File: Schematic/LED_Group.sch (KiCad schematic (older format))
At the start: 21 parts

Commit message: V1.1.0 Realized that while the TLS5940 PWM Driver chip is using the SPI MOSI and SCK signals, the full signaling isn't SPI compatable. Specifically, the latch signal is high active where SPI CS is low active. Removed the SPI cleverness that allows many SPI devices with only 2 CS pins and daisy-chaned all 26 TLS5940s. Also changed the I/O Expander from SPI to I2C. Still need to decide on how to properly handle the unused PWM Driver outputs to keep the internal constant current channels from trying to pump current through and open circuit. Maybe add back-side LEDs for status signals? Also need to watch out for problems driving that many drivers. Might need to split up the groups between multiple µPs. Never the less, should be ready for prototype stage at this point.
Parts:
- gave numbers to parts that had none: 19
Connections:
- net labels added: BLANK', GSCLK', SCK', SIN, SOUT, XLAT, XLAT', ~IR_LED
- net labels removed: IR_LED, MOSI, ~CS~/XLAT
- wire segments 71 -> 178
- no-connect marks 5 -> 9
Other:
- moved on the sheet: C201, C202, C203, D210, R201, R202, R203, U203

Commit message: 1.1.1 Change TIP120 to TIP31C (on-hand stock), change Cap Ref'ds on LED Groups Fritzing file to plan perfboard layout for LED groups.
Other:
- moved on the sheet: C1101, C1102, C1103

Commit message: Updated schematic for simplified auto-cycling leds. Lower part count and cost, not as flexible on color cycling.
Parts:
- removed C201, C202: 0.1µF, symbol CAP_NP
- removed D201, D202, D203, D204, D205, D206, D207, D208, D209: SparkFun COM-10821, symbol LED_RABG
- removed R201, R202: 1.91kΩ, symbol RES
- removed U201, U202: TLC5940NT, symbol TLC5940NT
- added D301, D302, D303, D304, D305, D306, D307, D308, D309: RGB Slow Flashing, symbol LED_Flashing
- added Q301: 2N2222, symbol Q_NPN_EBC
- added R301, R302, R303, R304, R305, R306, R307, R308, R309: 180Ω, symbol RES
- added R310: 1kΩ, symbol RES
- R311: renamed from R203; value 75Ω -> 180Ω
- renumbered C203 to C301, D210 to D310, U203 to U301
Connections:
- net labels added: Blue, Blue/White, Brown, Brown/White, Green, Green/White, IR_5V, IR_GND, LED, LED_5V, LED_GND1, LED_GND3, Orange, Orange/White
- net labels removed: BLANK, BLANK', GND, GSCLK, GSCLK', SCK, SCK', SIN, SOUT, XLAT, XLAT'
- wire segments 178 -> 52
- no-connect marks 9 -> 0
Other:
- note added: "LED Voltage Drop, 2.28V - 2.91V (Max current = 20mA)\n2N2222 Voltage Drop 17.8mV - 15.1mV\nResustor Voltage Drop 2.57 - 2.00V\n\nTarget current = 15mA for a total of 1.755A with 117 LEDs"
- moved on the sheet: C1101, D1110, R1111, U1101

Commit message: Change TIP31C to 2N2222. (Don't need the current capacity, so why pay for it?) Clean-up BOM items.
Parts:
- D301, D302, D303, D304, D305, D306, D307, D308, D309: CommonPartLibrary CPL-LED-RGP-CYCLING-SLOW* -> CPL-LED-RGB-CYCLING-SLOW*
- D310: CommonPartLibrary CPL-LED-5MM-IR -> CPL-LED-5MM-IR*
- R301, R302, R303, R304, R305, R306, R307, R308, R309: CommonPartLibrary CPL-RES-THT-180-0.25W -> CPL-RES-THT-180-0.25W*; MfgPart MFR-25FBF52-10R -> MFR-25FBF52-180R
- R310: MfgPart MFR-25FBF52-1k -> MFR-25FBF52-1K
- R311: CommonPartLibrary CPL-RES-THT-75.0-0.25W -> CPL-RES-THT-180-0.25W*; MfgPart MFR-25FBF52-75R -> MFR-25FBF52-180R
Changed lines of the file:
@@
 Sheet 11 15
 Title "Interactive Rainbow"
-Date "2015-12-05"
-Rev "1.2.0"
+Date "2015-12-06"
+Rev "1.2.1"
 Comp "Sembazuru Circuit (for Barrel of Makers)"
-Comment1 "1.0.0 Initial Circuit"
-Comment2 "1.1.0 TLC5940 isn't actually SPI. Removed SPI cleverness and change I/O expander to I2C"
-Comment3 "1.1.1 Change TIP120 to TIP31C (on-hand stock), change Cap Ref'ds on LED Groups"
-Comment4 "1.2.0 Change design to use LEDs with integrated flashing. Simpler design."
+Comment1 "1.1.0 TLC5940 isn't actually SPI. Removed SPI cleverness and change I/O expander to I2C"
+Comment2 "1.1.1 Change TIP120 to TIP31C (on-hand stock), change Cap Ref'ds on LED Groups"
+Comment3 "1.2.0 Change design to use LEDs with integrated flashing. Simpler design."
+Comment4 "1.2.1 Chance TIP31C to 2N2222. Don't need extra current capacity."
 $EndDescr
 Text HLabel 1050 4700 0    60   Input ~ 0
@@
 F 2 "" H 2100 4700 60  0001 C CNN
 F 3 "" H 2200 4800 60  0001 C CNN
-F 4 "CPL-LED-5MM-IR" H 2200 4700 60  0001 C CNN "CommonPartLibrary"
+F 4 "CPL-LED-5MM-IR*" H 2200 4700 60  0001 C CNN "CommonPartLibrary"
 F 5 "Vishay" H 2200 4700 60  0001 C CNN "Mfg"
 F 6 "TSUS5202" H 2200 4700 60  0001 C CNN "MfgPart"
@@
 F 2 "" H 3100 5350 60  0000 C CNN
 F 3 "" H 3100 5350 60  0000 C CNN
-F 4 "CPL-RES-THT-75.0-0.25W" H 3100 5350 60  0001 C CNN "CommonPartLibrary"
+F 4 "CPL-RES-THT-180-0.25W*" H 3100 5350 60  0001 C CNN "CommonPartLibrary"
 F 5 "Yageo" H 3100 5350 60  0001 C CNN "Mfg"
-F 6 "MFR-25FBF52-75R" H 3100 5350 60  0001 C CNN "MfgPart"
+F 6 "MFR-25FBF52-180R" H 3100 5350 60  0001 C CNN "MfgPart"
 	1    3100 5350
 	1    0    0    -1
@@
 F 2 "" H 5200 1800 60  0001 C CNN
 F 3 "" H 5300 1700 60  0001 C CNN
-F 4 "CPL-LED-RGP-CYCLING-SLOW*" H 5300 1650 60  0001 C CNN "CommonPartLibrary"
+F 4 "CPL-LED-RGB-CYCLING-SLOW*" H 5300 1650 60  0001 C CNN "CommonPartLibrary"
 F 5 "AdaFruit" H 5300 1650 60  0001 C CNN "Mfg"
 F 6 "ADA679" H 5300 1650 60  0001 C CNN "MfgPart"
@@
 F 4 "CPL-RES-THT-1k-0.25W" H 2800 2650 60  0001 C CNN "CommonPartLibrary"
 F 5 "Yageo" H 2800 2650 60  0001 C CNN "Mfg"
-F 6 "MFR-25FBF52-1k" H 2800 2650 60  0001 C CNN "MfgPart"
+F 6 "MFR-25FBF52-1K" H 2800 2650 60  0001 C CNN "MfgPart"
 	1    2800 2650
 	1    0    0    -1
@@
 F 2 "" H 5300 1050 60  0000 C CNN
 F 3 "" H 5300 1050 60  0000 C CNN
-F 4 "CPL-RES-THT-180-0.25W" H 5300 1050 60  0001 C CNN "CommonPartLibrary"
+F 4 "CPL-RES-THT-180-0.25W*" H 5300 1050 60  0001 C CNN "CommonPartLibrary"
 F 5 "Yageo" H 5300 1050 60  0001 C CNN "Mfg"
-F 6 "MFR-25FBF52-10R" H 5300 1050 60  0001 C CNN "MfgPart"
+F 6 "MFR-25FBF52-180R" H 5300 1050 60  0001 C CNN "MfgPart"
 	1    5300 1050
 	0    1    1    0
@@
 F 2 "" H 7200 1800 60  0001 C CNN
 F 3 "" H 7300 1700 60  0001 C CNN
-F 4 "CPL-LED-RGP-CYCLING-SLOW*" H 7300 1650 60  0001 C CNN "CommonPartLibrary"
+F 4 "CPL-LED-RGB-CYCLING-SLOW*" H 7300 1650 60  0001 C CNN "CommonPartLibrary"
 F 5 "AdaFruit" H 7300 1650 60  0001 C CNN "Mfg"
 F 6 "ADA679" H 7300 1650 60  0001 C CNN "MfgPart"
@@
 F 2 "" H 7300 1050 60  0000 C CNN
 F 3 "" H 7300 1050 60  0000 C CNN
-F 4 "CPL-RES-THT-180-0.25W" H 7300 1050 60  0001 C CNN "CommonPartLibrary"
+F 4 "CPL-RES-THT-180-0.25W*" H 7300 1050 60  0001 C CNN "CommonPartLibrary"
 F 5 "Yageo" H 7300 1050 60  0001 C CNN "Mfg"
-F 6 "MFR-25FBF52-10R" H 7300 1050 60  0001 C CNN "MfgPart"
+F 6 "MFR-25FBF52-180R" H 7300 1050 60  0001 C CNN "MfgPart"
 	1    7300 1050
 	0    1    1    0
@@
 F 2 "" H 9200 1800 60  0001 C CNN
 F 3 "" H 9300 1700 60  0001 C CNN
-F 4 "CPL-LED-RGP-CYCLING-SLOW*" H 9300 1650 60  0001 C CNN "CommonPartLibrary"
+F 4 "CPL-LED-RGB-CYCLING-SLOW*" H 9300 1650 60  0001 C CNN "CommonPartLibrary"
 F 5 "AdaFruit" H 9300 1650 60  0001 C CNN "Mfg"
 F 6 "ADA679" H 9300 1650 60  0001 C CNN "MfgPart"
@@
 F 2 "" H 9300 1050 60  0000 C CNN
 F 3 "" H 9300 1050 60  0000 C CNN
-F 4 "CPL-RES-THT-180-0.25W" H 9300 1050 60  0001 C CNN "CommonPartLibrary"
+F 4 "CPL-RES-THT-180-0.25W*" H 9300 1050 60  0001 C CNN "CommonPartLibrary"
 F 5 "Yageo" H 9300 1050 60  0001 C CNN "Mfg"
-F 6 "MFR-25FBF52-10R" H 9300 1050 60  0001 C CNN "MfgPart"
+F 6 "MFR-25FBF52-180R" H 9300 1050 60  0001 C CNN "MfgPart"
 	1    9300 1050
 	0    1    1    0
@@
 F 2 "" H 5200 3800 60  0001 C CNN
 F 3 "" H 5300 3700 60  0001 C CNN
-F 4 "CPL-LED-RGP-CYCLING-SLOW*" H 5300 3650 60  0001 C CNN "CommonPartLibrary"
+F 4 "CPL-LED-RGB-CYCLING-SLOW*" H 5300 3650 60  0001 C CNN "CommonPartLibrary"
 F 5 "AdaFruit" H 5300 3650 60  0001 C CNN "Mfg"
 F 6 "ADA679" H 5300 3650 60  0001 C CNN "MfgPart"
@@
 F 2 "" H 5300 3050 60  0000 C CNN
 F 3 "" H 5300 3050 60  0000 C CNN
-F 4 "CPL-RES-THT-180-0.25W" H 5300 3050 60  0001 C CNN "CommonPartLibrary"
+F 4 "CPL-RES-THT-180-0.25W*" H 5300 3050 60  0001 C CNN "CommonPartLibrary"
 F 5 "Yageo" H 5300 3050 60  0001 C CNN "Mfg"
-F 6 "MFR-25FBF52-10R" H 5300 3050 60  0001 C CNN "MfgPart"
+F 6 "MFR-25FBF52-180R" H 5300 3050 60  0001 C CNN "MfgPart"
 	1    5300 3050
 	0    1    1    0
@@
 F 2 "" H 7200 3800 60  0001 C CNN
 F 3 "" H 7300 3700 60  0001 C CNN
-F 4 "CPL-LED-RGP-CYCLING-SLOW*" H 7300 3650 60  0001 C CNN "CommonPartLibrary"
+F 4 "CPL-LED-RGB-CYCLING-SLOW*" H 7300 3650 60  0001 C CNN "CommonPartLibrary"
 F 5 "AdaFruit" H 7300 3650 60  0001 C CNN "Mfg"
 F 6 "ADA679" H 7300 3650 60  0001 C CNN "MfgPart"
@@
 F 2 "" H 7300 3050 60  0000 C CNN
 F 3 "" H 7300 3050 60  0000 C CNN
-F 4 "CPL-RES-THT-180-0.25W" H 7300 3050 60  0001 C CNN "CommonPartLibrary"
+F 4 "CPL-RES-THT-180-0.25W*" H 7300 3050 60  0001 C CNN "CommonPartLibrary"
 F 5 "Yageo" H 7300 3050 60  0001 C CNN "Mfg"
-F 6 "MFR-25FBF52-10R" H 7300 3050 60  0001 C CNN "MfgPart"
+F 6 "MFR-25FBF52-180R" H 7300 3050 60  0001 C CNN "MfgPart"
 	1    7300 3050
 	0    1    1    0
@@
 F 2 "" H 9200 3800 60  0001 C CNN
 F 3 "" H 9300 3700 60  0001 C CNN
-F 4 "CPL-LED-RGP-CYCLING-SLOW*" H 9300 3650 60  0001 C CNN "CommonPartLibrary"
+F 4 "CPL-LED-RGB-CYCLING-SLOW*" H 9300 3650 60  0001 C CNN "CommonPartLibrary"
 F 5 "AdaFruit" H 9300 3650 60  0001 C CNN "Mfg"
 F 6 "ADA679" H 9300 3650 60  0001 C CNN "MfgPart"
@@
 F 2 "" H 9300 3050 60  0000 C CNN
 F 3 "" H 9300 3050 60  0000 C CNN
-F 4 "CPL-RES-THT-180-0.25W" H 9300 3050 60  0001 C CNN "CommonPartLibrary"
+F 4 "CPL-RES-THT-180-0.25W*" H 9300 3050 60  0001 C CNN "CommonPartLibrary"
 F 5 "Yageo" H 9300 3050 60  0001 C CNN "Mfg"
-F 6 "MFR-25FBF52-10R" H 9300 3050 60  0001 C CNN "MfgPart"
+F 6 "MFR-25FBF52-180R" H 9300 3050 60  0001 C CNN "MfgPart"
 	1    9300 3050
 	0    1    1    0
@@
 F 2 "" H 5200 5800 60  0001 C CNN
 F 3 "" H 5300 5700 60  0001 C CNN
-F 4 "CPL-LED-RGP-CYCLING-SLOW*" H 5300 5650 60  0001 C CNN "CommonPartLibrary"
+F 4 "CPL-LED-RGB-CYCLING-SLOW*" H 5300 5650 60  0001 C CNN "CommonPartLibrary"
 F 5 "AdaFruit" H 5300 5650 60  0001 C CNN "Mfg"
 F 6 "ADA679" H 5300 5650 60  0001 C CNN "MfgPart"
@@
 F 2 "" H 5300 5050 60  0000 C CNN
 F 3 "" H 5300 5050 60  0000 C CNN
-F 4 "CPL-RES-THT-180-0.25W" H 5300 5050 60  0001 C CNN "CommonPartLibrary"
+F 4 "CPL-RES-THT-180-0.25W*" H 5300 5050 60  0001 C CNN "CommonPartLibrary"
 F 5 "Yageo" H 5300 5050 60  0001 C CNN "Mfg"
-F 6 "MFR-25FBF52-10R" H 5300 5050 60  0001 C CNN "MfgPart"
+F 6 "MFR-25FBF52-180R" H 5300 5050 60  0001 C CNN "MfgPart"
 	1    5300 5050
 	0    1    1    0
@@
 F 2 "" H 7200 5800 60  0001 C CNN
 F 3 "" H 7300 5700 60  0001 C CNN
-F 4 "CPL-LED-RGP-CYCLING-SLOW*" H 7300 5650 60  0001 C CNN "CommonPartLibrary"
+F 4 "CPL-LED-RGB-CYCLING-SLOW*" H 7300 5650 60  0001 C CNN "CommonPartLibrary"
 F 5 "AdaFruit" H 7300 5650 60  0001 C CNN "Mfg"
 F 6 "ADA679" H 7300 5650 60  0001 C CNN "MfgPart"
@@
 F 2 "" H 7300 5050 60  0000 C CNN
 F 3 "" H 7300 5050 60  0000 C CNN
-F 4 "CPL-RES-THT-180-0.25W" H 7300 5050 60  0001 C CNN "CommonPartLibrary"
+F 4 "CPL-RES-THT-180-0.25W*" H 7300 5050 60  0001 C CNN "CommonPartLibrary"
 F 5 "Yageo" H 7300 5050 60  0001 C CNN "Mfg"
-F 6 "MFR-25FBF52-10R" H 7300 5050 60  0001 C CNN "MfgPart"
+F 6 "MFR-25FBF52-180R" H 7300 5050 60  0001 C CNN "MfgPart"
 	1    7300 5050
 	0    1    1    0
@@
 F 2 "" H 9200 5800 60  0001 C CNN
 F 3 "" H 9300 5700 60  0001 C CNN
-F 4 "CPL-LED-RGP-CYCLING-SLOW*" H 9300 5650 60  0001 C CNN "CommonPartLibrary"
+F 4 "CPL-LED-RGB-CYCLING-SLOW*" H 9300 5650 60  0001 C CNN "CommonPartLibrary"
 F 5 "AdaFruit" H 9300 5650 60  0001 C CNN "Mfg"
 F 6 "ADA679" H 9300 5650 60  0001 C CNN "MfgPart"
@@
 F 2 "" H 9300 5050 60  0000 C CNN
 F 3 "" H 9300 5050 60  0000 C CNN
-F 4 "CPL-RES-THT-180-0.25W" H 9300 5050 60  0001 C CNN "CommonPartLibrary"
+F 4 "CPL-RES-THT-180-0.25W*" H 9300 5050 60  0001 C CNN "CommonPartLibrary"
 F 5 "Yageo" H 9300 5050 60  0001 C CNN "Mfg"
-F 6 "MFR-25FBF52-10R" H 9300 5050 60  0001 C CNN "MfgPart"
+F 6 "MFR-25FBF52-180R" H 9300 5050 60  0001 C CNN "MfgPart"
 	1    9300 5050
 	0    1    1    0

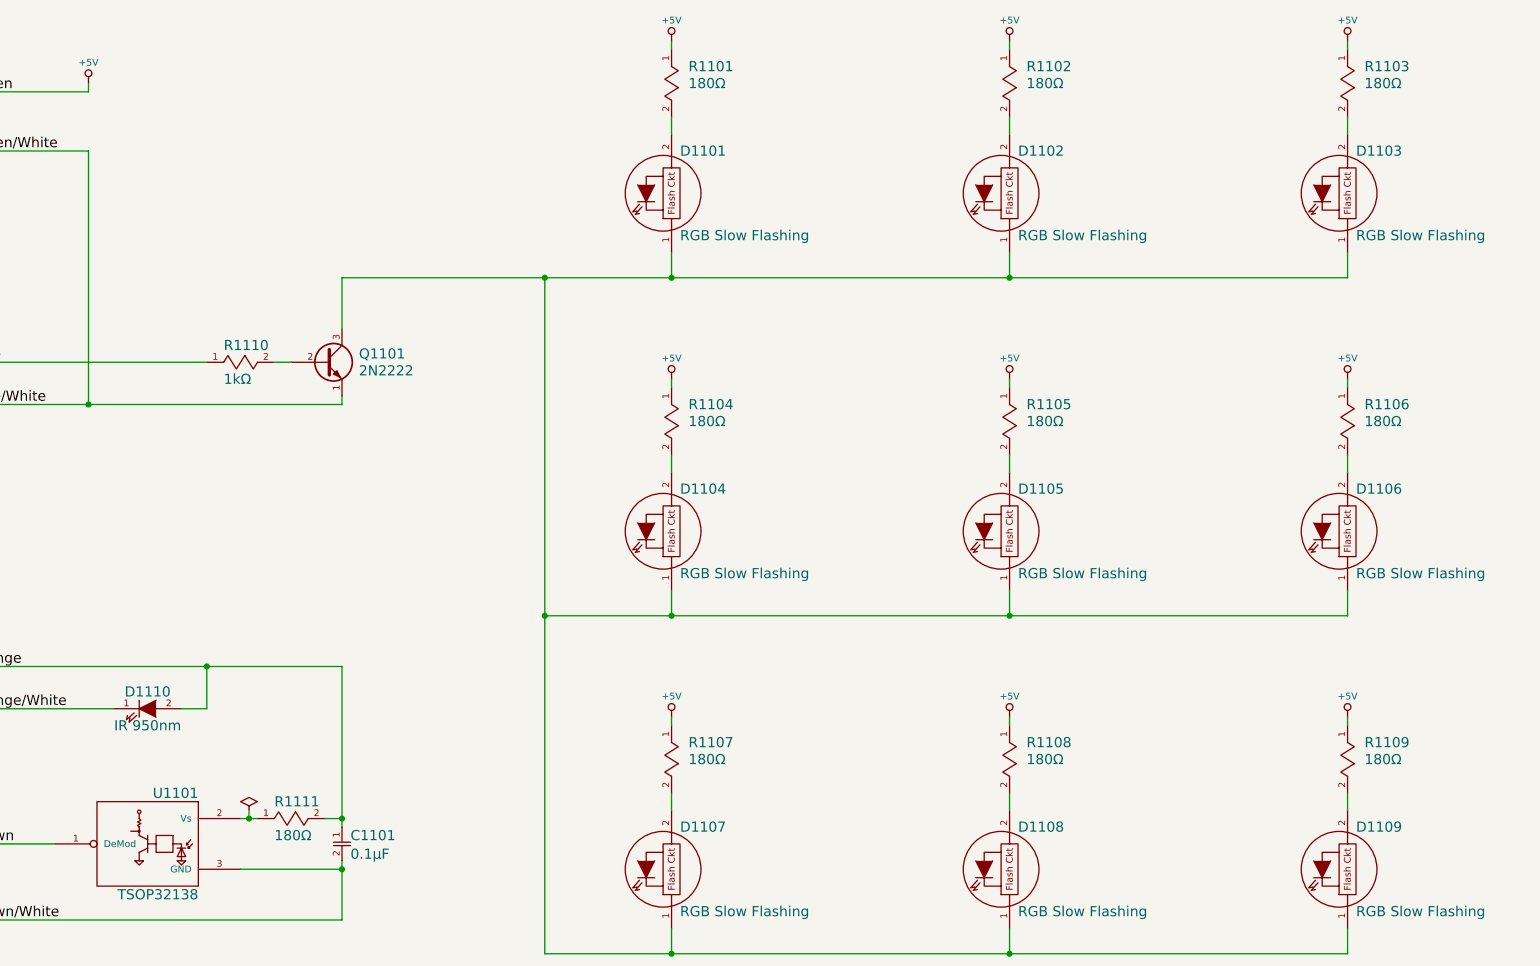
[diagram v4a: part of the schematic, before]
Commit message: v1.2.2 Change 555 to CMOS 7555 to simplify IR strobe design & lower current. And, control IR LEDs to only light when SPI transfer.
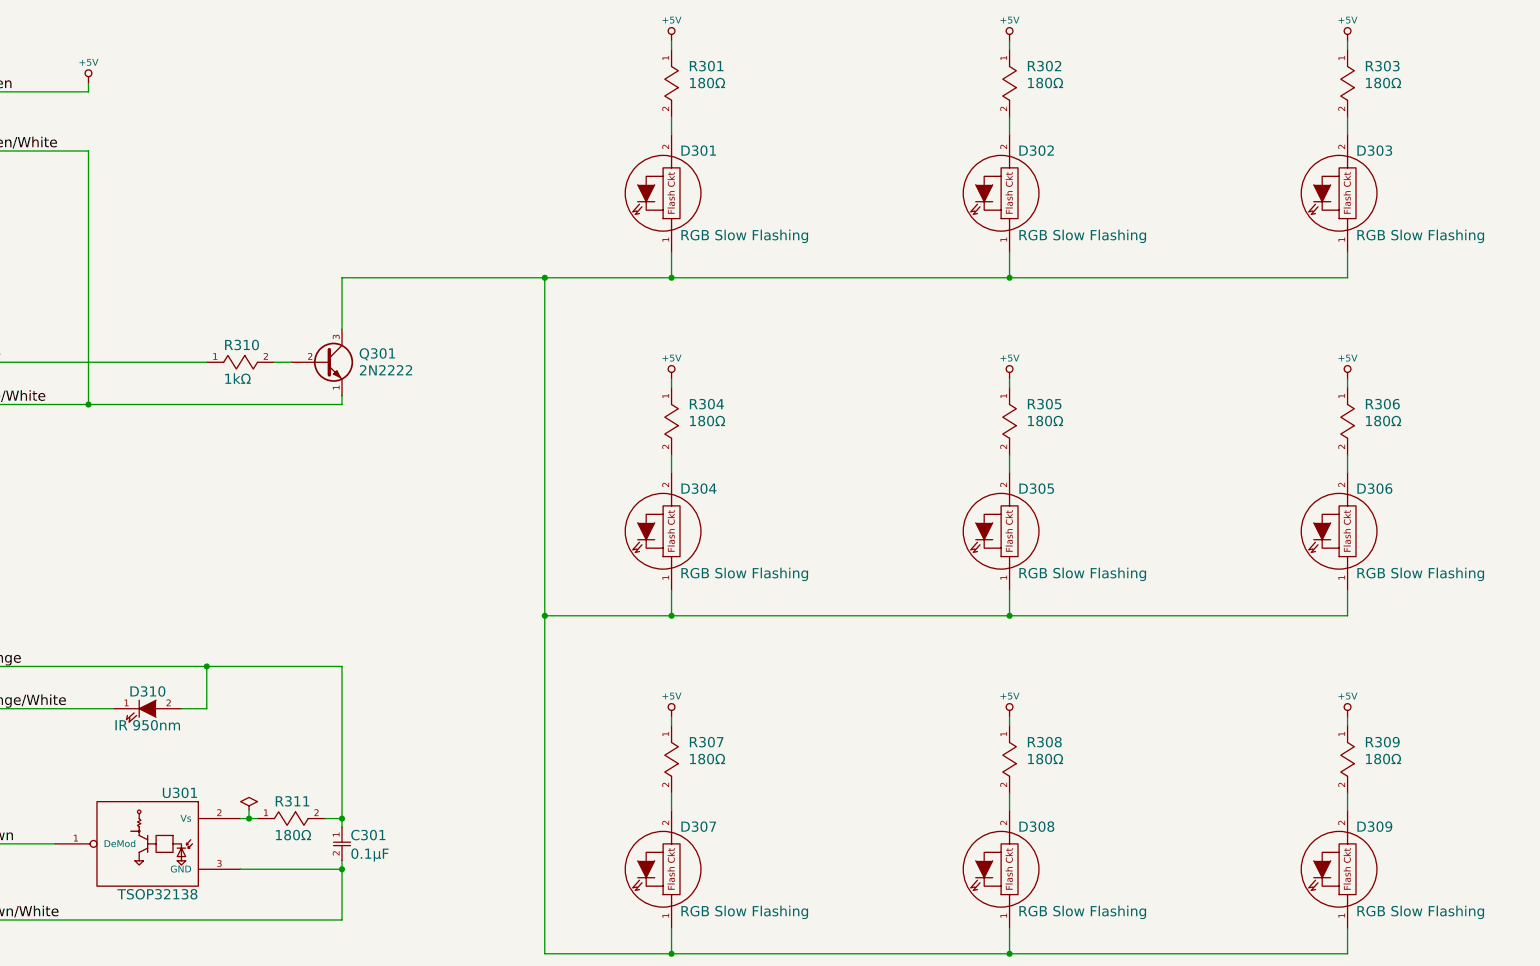
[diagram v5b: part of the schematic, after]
